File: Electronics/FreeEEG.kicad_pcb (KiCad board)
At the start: 2 copper layers, 56.3 x 91.6 mm, 119 parts, among them J1 ConnElectrodes, J2 10137065-00021LF, Q1 2N7002, Q2 2N7002, Q3 2N7002, SW1 ON_SW, SW2 SEL_SW, SW3 RST_BTN, SW4 BOOT_BTN, U1 ADS1299, U2 OPA376xxDBV, U3 ESP32-S3-WROOM-1, U4 OPA376xxDBV, U5 XL1509-3.3, U6 NCP1117-5.0_SOT223, U7 MPU-6050

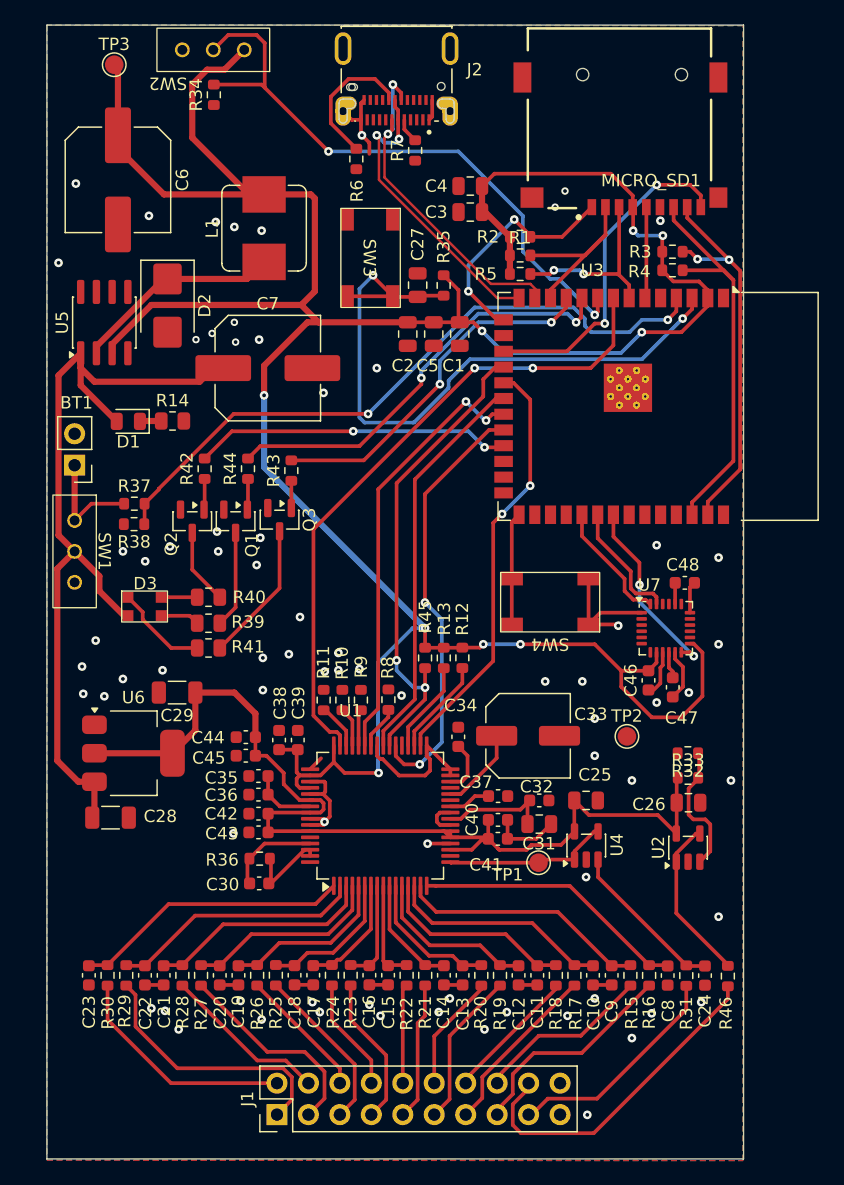
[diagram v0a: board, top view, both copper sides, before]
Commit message: New board release and adding support for ws2812 LED
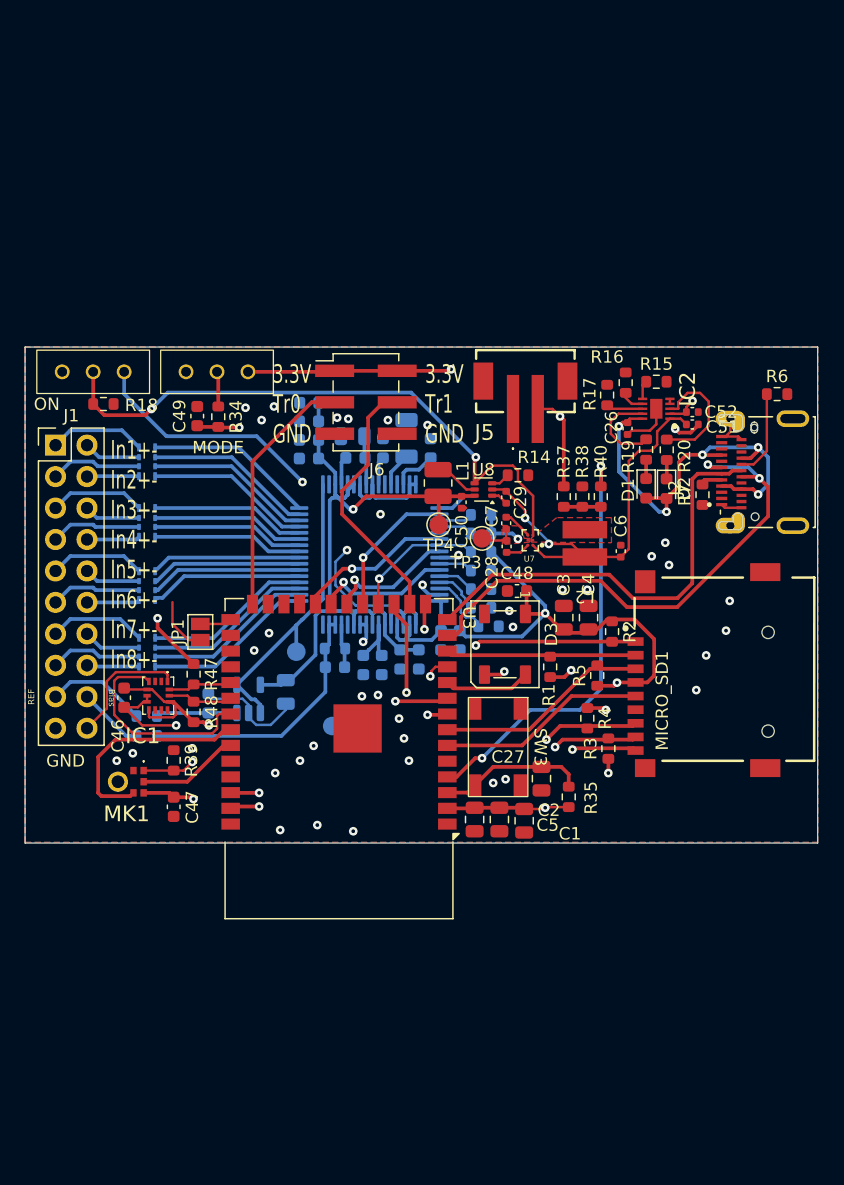
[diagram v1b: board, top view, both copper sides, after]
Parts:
- removed BT1: 9V, Connector_PinHeader_2.54mm:PinHeader_1x02_P2.54mm_Vertical
- removed C10, C11, C12, C13, C14, C15, C16, C17, C18, C19, C20, C21, C22, C23, C8, C9: 4.7n, Capacitor_SMD:C_0603_1608Metric
- removed Q1, Q2, Q3: 2N7002, Package_TO_SOT_SMD:SOT-23
- removed R21, R22, R23, R24, R25, R26, R27, R28, R29, R30, R46: 4.99k, Resistor_SMD:R_0603_1608Metric
- removed R32, R33: 2M, Resistor_SMD:R_0603_1608Metric
- removed R41: 610, Resistor_SMD:R_0805_2012Metric
- removed R42, R43, R44: 10, Resistor_SMD:R_0603_1608Metric
- removed SW4: BOOT_BTN, K2-1187SQ-A4SW-06:K2-1187SQ-A4SW-06
- removed U2: OPA376xxDBV, Package_TO_SOT_SMD:SOT-23-5
- removed U5: XL1509-3.3, Package_SO:SOIC-8_3.9x4.9mm_P1.27mm
- removed U6: NCP1117-5.0_SOT223, Package_TO_SOT_SMD:SOT-223-3_TabPin2
- added C49: 1u, Capacitor_SMD:C_0603_1608Metric, F.Cu at (133.9, 95.6)
- added C50: 10u, Capacitor_SMD:C_0402_1005Metric, F.Cu at (155.2, 102.5)
- added C51: 10u, Capacitor_SMD:C_0402_1005Metric, F.Cu at (173.9, 96.2)
- added C52: 1u, Capacitor_SMD:C_0402_1005Metric, F.Cu at (173.9, 95.2)
- added IC1: ICM-42670-P, ICM-42670-P:ICM42670P, F.Cu at (130.8, 118.2)
- added IC2: BQ25185DLHR, BQ25185DLHR:SON40P220X200X80-11N, F.Cu at (171.0, 95.0)
- added J5: B2B-PH-SM4-TBT_LF, B2B-PH-SM4-TBT_LF__SN_:B2BPHSM4TBTLFSN, F.Cu at (160.4, 92.8)
- added J6: ExtTrig, Connector_PinHeader_2.54mm:PinHeader_2x03_P2.54mm_Vertical_SMD, F.Cu at (147.5, 94.5)
- added JP1: BOOT_JUMPER, Jumper:SolderJumper-2_P1.3mm_Open_Pad1.0x1.5mm, F.Cu at (134.2, 113.0)
- added L2: 2.2u, PIS2D18LP:PIS2D18LP, F.Cu at (165.2, 105.8)
- added MK1: ICS-43434, ICS-43434:ICS43434, F.Cu at (128.2, 125.1)
- added R47: 4.7k, Resistor_SMD:R_0603_1608Metric, F.Cu at (133.6, 116.4)
- added R48: 4.7k, Resistor_SMD:R_0603_1608Metric, F.Cu at (133.6, 119.5)
- added R49: 4.99k, Resistor_SMD:R_0603_1608Metric, B.Cu at (129.8, 121.4)
- added RN1: R_Pack04_SIP_Split, 4D03WGF5101T5E:4D03WGF5101T5E, B.Cu at (129.8, 99.3)
- added RN2: R_Pack04_SIP_Split, 4D03WGF5101T5E:4D03WGF5101T5E, B.Cu at (129.8, 104.2)
- added RN3: R_Pack04_SIP_Split, 4D03WGF5101T5E:4D03WGF5101T5E, B.Cu at (129.8, 109.3)
- added RN4: R_Pack04_SIP_Split, 4D03WGF5101T5E:4D03WGF5101T5E, B.Cu at (129.8, 114.7)
- added TP4: 5V_TEST, TestPoint:TestPoint_Pad_D1.5mm, F.Cu at (153.4, 104.3)
- added U8: TPS628438DRL, Package_TO_SOT_SMD:SOT-563, F.Cu at (157.0, 101.5)
- C24, C25, C30, C31, C32, C34, C35, C36, C37, C38, C39, C40, C41, C42, C43, C44, C45, R10, R11, R12, R13, R31, R36, R45, R8, R9, TP1, TP2, U1, U4: moved to B.Cu
- C26: footprint Capacitor_SMD:C_0805_2012Metric -> Capacitor_SMD:C_0402_1005Metric
- C28: value 33u -> 10u; footprint Capacitor_SMD:C_1206_3216Metric -> Capacitor_SMD:C_0402_1005Metric
- C29: value 33u -> 4.7u; footprint Capacitor_SMD:C_1206_3216Metric -> Capacitor_SMD:C_0402_1005Metric
- C33: footprint Capacitor_SMD:C_Elec_6.3x7.7 -> Capacitor_SMD:C_1206_3216Metric; moved to B.Cu
- C47: value 100n -> 10n
- C48: value 2.2n -> 10n
- C6: value 330u -> 10u; footprint Capacitor_SMD:C_Elec_8x10.2 -> Capacitor_SMD:C_0402_1005Metric
- C7: value 470u -> 10u; footprint Capacitor_SMD:C_Elec_8x10.2 -> Capacitor_SMD:C_0402_1005Metric
- D1: value ON_LED -> LED_AMBAR; footprint LED_SMD:LED_0805_2012Metric -> LED_SMD:LED_0603_1608Metric
- D2: value SS54B -> LED_BLUE; footprint Diode_SMD:D_SMB -> LED_SMD:LED_0603_1608Metric
- D3: value LED_RAGB -> WS2812B; footprint XL-3528RGBW-HM:XL-3528RGBW-HM -> LED_SMD:LED_WS2812B_PLCC4_5.0x5.0mm_P3.2mm
- L1: value 47u -> 1u; footprint Inductor_SMD:L_Bourns_SRP7028A_7.3x6.6mm -> Inductor_SMD:L_1008_2520Metric
- R14: value 400 -> 249k; footprint Resistor_SMD:R_0805_2012Metric -> Resistor_SMD:R_0603_1608Metric
- R15: value 4.99k -> 10k
- R16: value 4.99k -> 13k
- R17: value 4.99k -> 619
- R18: value 4.99k -> 22k
- R19: value 4.99k -> 150
- R20: value 4.99k -> 120
- R34: value 33k -> 50k
- R38: value 1M -> 2M
- R39: value 720 -> 100k; footprint Resistor_SMD:R_0805_2012Metric -> Resistor_SMD:R_0603_1608Metric
- R40: value 610 -> 10k; footprint Resistor_SMD:R_0805_2012Metric -> Resistor_SMD:R_0603_1608Metric
- U7: value MPU-6050 -> TPS610997YFFR; footprint Sensor_Motion:InvenSense_QFN-24_4x4mm_P0.5mm -> TPS610997YFFR:BGA6N40P3X2_122X88X62N
- moved R18 58.8 mm to (126.3, 94.6), turned to 0 degrees
- moved J1 56.9 mm to (122.5, 97.9), turned to 0 degrees
- moved C6 50.5 mm to (168.1, 106.5), turned to 90 degrees
- moved TP3 48.4 mm to (156.9, 105.5), turned to -90 degrees
- moved R31 48.3 mm to (129.8, 119.8), turned to 180 degrees
- moved R15 48.0 mm to (171.0, 92.8), turned to 0 degrees
- moved R16 47.9 mm to (168.5, 92.9), turned to 90 degrees
- moved R17 46.9 mm to (167.0, 93.9), turned to 90 degrees
- moved J2 46.8 mm to (182.0, 100.1), turned to 90 degrees
- moved C24 45.7 mm to (134.8, 118.8), turned to 90 degrees
- moved MICRO_SD1 45.3 mm to (176.5, 116.0), turned to 90 degrees
- moved R20 45.0 mm to (171.8, 98.3), turned to 90 degrees
- moved R19 44.1 mm to (170.2, 98.3), turned to 90 degrees
- moved D2 42.9 mm to (171.8, 101.4)
- moved R35 42.5 mm to (163.9, 126.3), turned to 90 degrees
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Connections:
- net Net-(U1-BIASIN) renamed /Analog/BIAS_OUT
- C26 pad 2: +5V -> VBUS
- C28 pad 1: BATT -> +3.3V
- C29 pad 1: +5V -> BATT
- C47 pad 2: Net-(U7-REGOUT) -> +3.3V
- C48 pad 2: Net-(U7-CPOUT) -> +3.3V
- C6 pad 1: +3.3V -> BATT
- C7 pad 1: BATT -> +3.3V
- D1 pad 2: BATT -> VBUS
- D2 pad 2: GND -> VBUS
- D3 pad 1: Net-(D3-RK) -> +3.3V
- D3 pad 2: BATT -> unconnected-(D3-DOUT-Pad2)
- D3 pad 3: Net-(D3-GK) -> GND
- D3 pad 4: Net-(D3-BK) -> LED
- J1 pad 1: IN8P -> IN1P
- J1 pad 10: IN4N -> IN5N
- J1 pad 11: IN3P -> IN6P
- J1 pad 12: IN3N -> IN6N
- J1 pad 13: IN2P -> IN7P
- J1 pad 14: IN2N -> IN7N
- J1 pad 15: IN1P -> IN8P
- J1 pad 16: IN1N -> IN8N
- J1 pad 2: IN8N -> IN1N
- J1 pad 3: IN7P -> IN2P
- J1 pad 4: IN7N -> IN2N
- J1 pad 5: IN6P -> IN3P
- J1 pad 6: IN6N -> IN3N
- J1 pad 7: IN5P -> IN4P
- J1 pad 8: IN5N -> IN4N
- J1 pad 9: IN4P -> IN5P
- J2 pad A4: VBUS_A_1 -> VBUS
- J2 pad A9: VBUS_A -> VBUS
- J2 pad B4: VBUS_B_1 -> VBUS
- J2 pad B9: VBUS_B -> VBUS
- L1 pad 1: Net-(D2-K) -> Net-(U8-SW)
- L1 pad 2: +3.3V -> +5V
- R14 pad 1: Net-(D1-K) -> Net-(U8-VSET)
- R15 pad 1: FIN1N -> Net-(IC2-TS/MR)
- R15 pad 2: IN1N -> GND
- R16 pad 1: FIN1P -> Net-(IC2-ILIM/VSET)
- R16 pad 2: IN1P -> GND
- R17 pad 1: FIN2P -> Net-(IC2-ISET)
- R17 pad 2: IN2P -> GND
- R18 pad 1: FIN2N -> SYS_EN
- R18 pad 2: IN2N -> GND
- R19 pad 1: FIN3P -> Net-(D1-K)
- R19 pad 2: IN3P -> BAT_STAT1
- R20 pad 1: FIN3N -> Net-(D2-K)
- R20 pad 2: IN3N -> BAT_STAT2
- R34 pad 1: GND -> Net-(SW2-B)
- R37 pad 2: BAT_MON -> Net-(R37-Pad2)
- R38 pad 1: BAT_MON -> Net-(R37-Pad2)
- R39 pad 1: /RED -> GND
- R39 pad 2: Net-(D3-RK) -> I2S_WS
- R40 pad 1: /GREEN -> BAT_MON
- R40 pad 2: Net-(D3-GK) -> Net-(R37-Pad2)
- SW1 pad 1: +BATT -> BATT
- SW1 pad 2: BATT -> SYS_EN
- SW2 pad 2: SEL -> Net-(SW2-B)
- SW2 pad 3: unconnected-(SW2-C-Pad3) -> GND
- U3 pad 10: LED_R -> LED
- U3 pad 11: LED_G -> I2S_WS
- U3 pad 16: unconnected-(U3-IO46-Pad16) -> TRIG1
- U3 pad 23: LED_B -> unconnected-(U3-IO21-Pad23)
- U3 pad 26: unconnected-(U3-IO45-Pad26) -> TRIG0
- U3 pad 34: unconnected-(U3-IO41-Pad34) -> I2S_CLK
- U3 pad 35: unconnected-(U3-IO42-Pad35) -> I2S_DATA
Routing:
- net +3.3V: track 241.2 -> 108.1 mm, vias 9 -> 11
- net SYS_EN: track 0.00 -> 48.9 mm, vias 0 -> 2
- net RESET: track 54.2 -> 12.0 mm, vias 2 -> 0
- net AFE_NDRDY: track 52.9 -> 14.6 mm
- net VBUS: track 0.00 -> 35.0 mm, vias 0 -> 5
- net LED_R: track 34.4 -> 0.00 mm, vias 2 -> 0
- net LED_G: track 29.2 -> 0.00 mm, vias 2 -> 0
- net I2S_WS: track 0.00 -> 28.2 mm, vias 0 -> 2
- net AFE_NCS: track 38.8 -> 10.9 mm, vias 2 -> 1
- net LED_B: track 25.6 -> 0.00 mm, vias 2 -> 0
- net AFE_DOUT: track 35.0 -> 11.3 mm, vias 2 -> 1
- net +5V: track 83.3 -> 60.3 mm, vias 0 -> 1
- net AFE_DIN: track 34.3 -> 11.4 mm, vias 2 -> 1
- net AFE_START: track 34.7 -> 12.6 mm, vias 2 -> 1
- net AFE_SCLK: track 32.4 -> 10.7 mm, vias 0 -> 1
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- added copper zone on F.Cu, net +3.3V
- added copper zone on In1.Cu, net +3.3V
- added copper zone on In2.Cu, net GND
- added copper zone on F.Cu, net Net-(U7-SW)
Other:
- board size 56.3 x 91.6 mm -> 64 x 40.1 mm
- copper layers 2 -> 4
- board text added: "3.3V Tr0 GND"
- board text added: "3.3V Tr1 GND"
- board text added: "Bias"
- board text added: "GND"
- board text added: "In1+- In2+- In3+- In4+- In5+- In6+- In7+- In8+-"
- board text added: "MODE"
- board text added: "ON"
- board text added: "REF"

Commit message: [Electronics] version 1.0.0 of the PCB released.\n [Firmware] Added ICS43434 drivers and prepared code for reestructuration
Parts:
- removed J5: B2B-PH-SM4-TBT_LF, B2B-PH-SM4-TBT_LF__SN_:B2BPHSM4TBTLFSN
- added J3: Conn_I2C, Connector_JST:JST_SH_SM04B-SRSS-TB_1x04-1MP_P1.00mm_Horizontal, F.Cu at (180.7, 130.0)
- added J4: battery_conn, Connector_Molex:Molex_PicoBlade_53261-0371_1x03-1MP_P1.25mm_Horizontal, F.Cu at (160.6, 93.0)
- TP3: value 3V3_TEST -> 5V_TEST
- TP4: value 5V_TEST -> 3V3_TEST
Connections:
- C28 pad 1: +3.3V -> +5V
- C50 pad 1: +5V -> +3.3V
- C7 pad 1: +3.3V -> +5V
- L1 pad 2: +5V -> +3.3V
- TP3 pad 1: +3.3V -> +5V
- TP4 pad 1: +5V -> +3.3V
- U3 pad 23: unconnected-(U3-IO21-Pad23) -> I2C_SDA
- U3 pad 5: unconnected-(U3-IO5-Pad5) -> I2C_SCL
- U7 pad B2: +3.3V -> +5V
- U8 pad 6: +5V -> +3.3V
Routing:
- net I2C_SDA: track 0.00 -> 50.3 mm, vias 0 -> 2
- net I2C_SCL: track 0.00 -> 29.4 mm, vias 0 -> 2
- net +3.3V: track 108.1 -> 130.2 mm
- net +5V: track 60.3 -> 66.1 mm
- net +BATT: track 21.5 -> 20.9 mm
- net GND: track 81.7 -> 82.2 mm, vias 43 -> 45
- added copper zone on F.Cu, net +5V
- removed copper zone on F.Cu, net +3.3V
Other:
- board size 64 x 40.1 mm -> 64 x 46.1 mm
